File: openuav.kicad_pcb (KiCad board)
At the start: 4 copper layers, 36 x 36 mm, 68 parts, among them J1 Conn_01x01, J10 Conn_01x01, J11 Conn_01x01, J12 Conn_01x01, J13 Conn_01x01, J14 Conn_01x01, J19 Conn_01x01, J2 Conn_01x01, J20 Conn_01x01, J21 Conn_01x01, J22 Conn_01x01, J23 Conn_01x01, J24 Conn_01x01, J25 Conn_01x01, J3 Conn_01x01, J30 Conn_01x01, J31 Conn_01x01, J4 Conn_01x01, J5 Conn_01x01, J6 Conn_01x01, J7 Conn_01x01, J8 Conn_01x01, J9 Conn_01x01, J99 USB_C_Receptacle_USB2.0, SW1 SW_Push, SW2 SW_Push, U1 STM32G431CBUx, U2 LPS22HH, U3 LSM6DSR, U4 TPS54302, U6 W25N01GVZEIG, U7 TLV75733PDBV

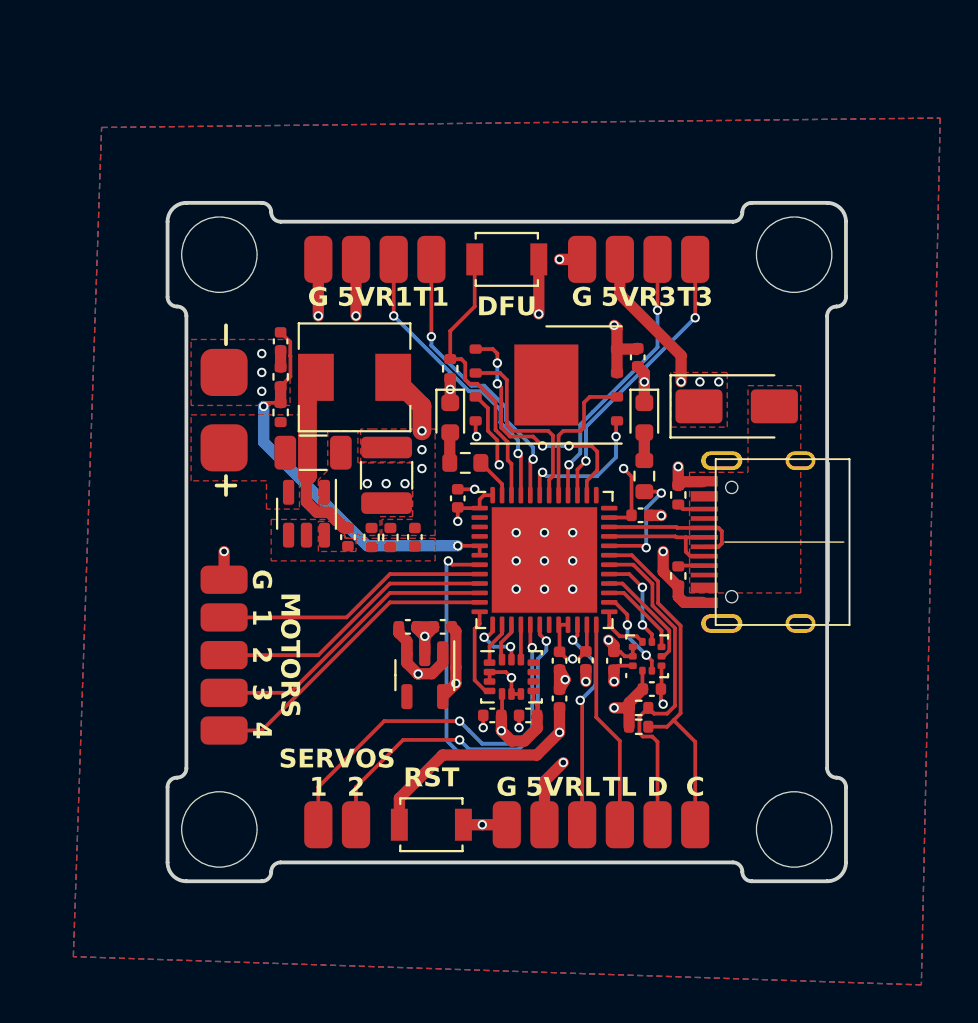
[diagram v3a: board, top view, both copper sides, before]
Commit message: Add dual 9v / 5v power supplies
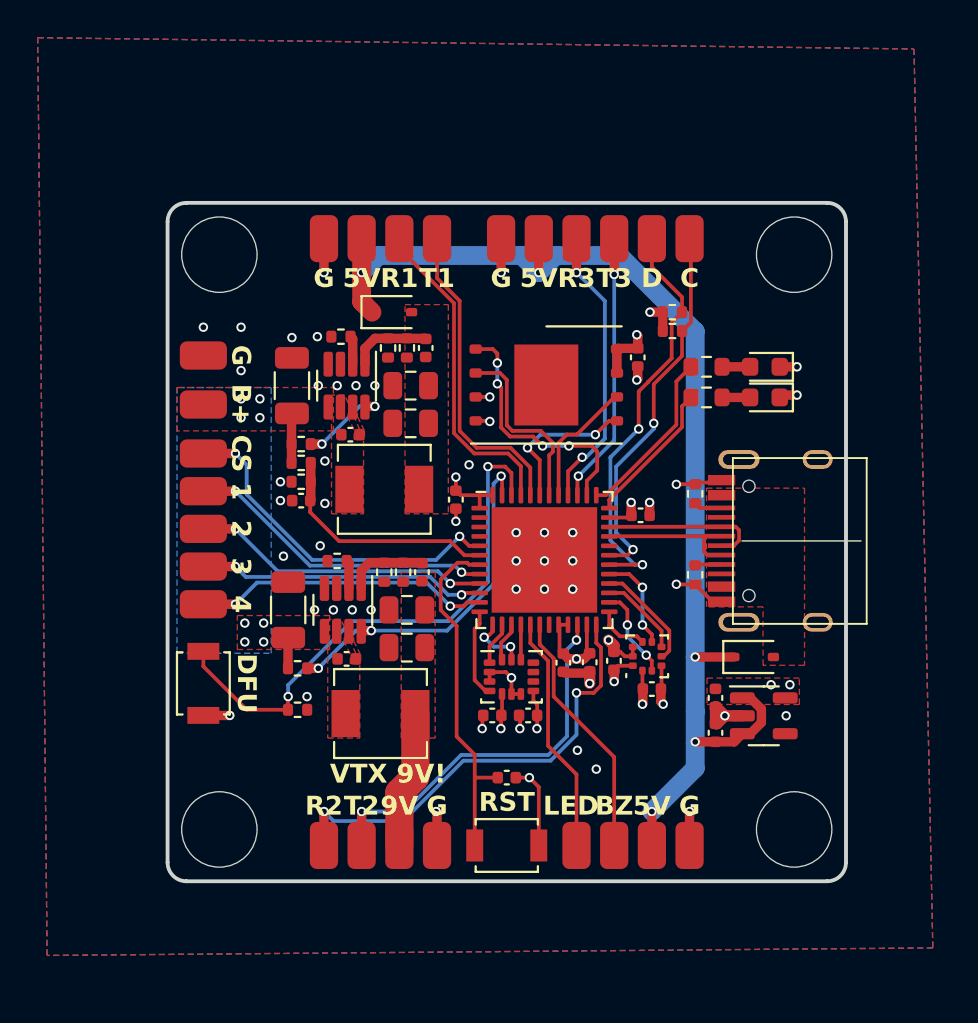
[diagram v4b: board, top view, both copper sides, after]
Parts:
- removed J30, J31: Conn_01x01, footprints:largepad
- added C17: 22u, Capacitor_SMD:C_0805_2012Metric, F.Cu at (142.7, 73.6)
- added C18: 100p, Capacitor_SMD:C_0402_1005Metric, F.Cu at (143.7, 57.7)
- added C19: 100p, Capacitor_SMD:C_0402_1005Metric, F.Cu at (143.5, 69.6)
- added C20: 22u, Capacitor_SMD:C_0805_2012Metric, F.Cu at (142.9, 61.7)
- added C21: 22u, Capacitor_SMD:C_0805_2012Metric, F.Cu at (142.7, 71.6)
- added C8: 10n, Capacitor_SMD:C_0402_1005Metric, F.Cu at (139.7, 62.3)
- added D4: PMEG2020AEA, Diode_SMD:D_SOD-323, F.Cu at (141.9, 55.8)
- added J15: Conn_01x01, footprints:smallpad, F.Cu at (131.9, 60.7)
- added J16: Conn_01x01, footprints:smallpad, F.Cu at (131.9, 58.1)
- added J17: Conn_01x01, footprints:smallpad, F.Cu at (142.3, 84.1)
- added J18: Conn_01x01, footprints:smallpad, F.Cu at (131.9, 63.3)
- added L2: 6.8u, Inductor_SMD:L_Sunlord_MWSA0402S, F.Cu at (141.3, 77.1)
- added R13: 47k, Resistor_SMD:R_0402_1005Metric, F.Cu at (139.0, 69.0)
- added R14: 100k, Resistor_SMD:R_0402_1005Metric, F.Cu at (142.5, 69.6)
- added R15: R, Resistor_SMD:R_0402_1005Metric, F.Cu at (141.5, 69.6)
- added R16: 10k, Resistor_SMD:R_0402_1005Metric, F.Cu at (137.1, 62.8)
- added R17: 10k, Resistor_SMD:R_0402_1005Metric, F.Cu at (136.9, 74.7)
- added R5: R, Resistor_SMD:R_0402_1005Metric, F.Cu at (141.7, 57.7)
- added U5: SY8303, Package_TO_SOT_SMD:TSOT-23-8, F.Cu at (139.3, 71.6)
- C10: value 68p -> 10u; footprint Capacitor_SMD:C_0402_1005Metric -> Capacitor_SMD:C_1206_3216Metric
- C15: value 47u -> 10n; footprint Capacitor_SMD:C_1210_3225Metric -> Capacitor_SMD:C_0402_1005Metric
- C9: value 100n -> 22u; footprint Capacitor_SMD:C_0402_1005Metric -> Capacitor_SMD:C_0805_2012Metric
- D1: value SS34 -> PMEG2020AEA; footprint Diode_SMD:D_SMA -> Diode_SMD:D_SOD-323
- L1: value 10u -> 6.8u; footprint Inductor_SMD:L_Sunlord_MWSA0503S -> Inductor_SMD:L_Sunlord_MWSA0402S
- R3: value 100k -> 47k
- R4: value 13.3k -> 100k
- U4: value TPS54302 -> SY8303; footprint Package_TO_SOT_SMD:SOT-23-6 -> Package_TO_SOT_SMD:TSOT-23-8
- moved J8 36.8 mm to (138.3, 84.1)
- moved J7 34.8 mm to (140.3, 84.1)
- moved J5 31.6 mm to (157.7, 84.1), turned to -90 degrees
- moved J6 31.1 mm to (155.7, 84.1), turned to -90 degrees
- moved J10 31.1 mm to (149.7, 51.9)
- moved J11 31.1 mm to (151.7, 51.9)
- moved J12 31.1 mm to (153.7, 51.9)
- moved J19 31.1 mm to (155.7, 51.9)
- moved J20 31.1 mm to (157.7, 51.9)
- moved J9 31.1 mm to (147.7, 51.9)
- moved SW1 27.7 mm to (131.9, 75.5), turned to 90 degrees
- moved R10 21.1 mm to (156.8, 56.8)
- moved R9 21.1 mm to (156.8, 55.8)
- moved R8 19.8 mm to (136.9, 76.9), turned to 0 degrees
- moved U7 18.1 mm to (161.6, 77.2), turned to 0 degrees
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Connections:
- C10 pad 1: Net-(U4-FB) -> +BATT
- C10 pad 2: +5V -> GND
- C15 pad 1: +5V -> Net-(U5-BS)
- C15 pad 2: GND -> Net-(U5-LX)
- C9 pad 1: Net-(U4-BOOT) -> Net-(D4-A)
- C9 pad 2: Net-(U4-SW) -> GND
- J11 pad 1: UART_4_RX -> UART_3_RX
- J12 pad 1: UART_4_TX -> UART_3_TX
- J7 pad 1: UART_3_RX -> UART_4_RX
- J8 pad 1: UART_3_TX -> UART_4_TX
- L1 pad 1: Net-(U4-SW) -> Net-(U4-LX)
- L1 pad 2: +5V -> Net-(D4-A)
- R3 pad 1: +5V -> Net-(U4-FS)
- R3 pad 2: Net-(U4-FB) -> GND
- R4 pad 1: Net-(U4-FB) -> Net-(D4-A)
- R4 pad 2: GND -> Net-(U4-FB)
- U1 pad 32: LED2 -> unconnected-(U1-PA10-Pad32)
- U1 pad 36: SWDIO -> LED2
- U1 pad 37: SWCLK -> LED1
- U1 pad 47: LED1 -> 9VEN
- U1 pad 5: VOLTAGE -> CURRENT
- U4 pad 1: GND -> Net-(U4-FB)
- U4 pad 2: Net-(U4-SW) -> Net-(U4-FS)
- U4 pad 3: +BATT -> GND
- U4 pad 4: Net-(U4-FB) -> GND
- U4 pad 5: unconnected-(U4-EN-Pad5) -> +BATT
- U4 pad 6: Net-(U4-BOOT) -> Net-(U4-LX)
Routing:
- net +5V: track 23.0 -> 64.4 mm, vias 9 -> 5
- net 9VEN: track 0.00 -> 19.1 mm, vias 0 -> 3
- net CURRENT: track 0.00 -> 18.7 mm, vias 0 -> 2
- net +3V3: track 39.2 -> 24.7 mm, vias 10 -> 13
- net BOOT0: track 15.0 -> 29.1 mm, vias 0 -> 2
- net UART_4_TX: track 11.1 -> 24.3 mm, vias 0 -> 2
- net NRST: track 30.8 -> 18.6 mm, vias 2 -> 0
- net UART_4_RX: track 11.6 -> 20.5 mm
- net VOLTAGE: track 21.3 -> 12.6 mm, vias 2 -> 0
- net Net-(U4-SW): track 8.70 -> 0.00 mm
- net PWM_5: track 21.2 -> 12.7 mm, vias 2 -> 0
- net +9V: track 0.00 -> 7.35 mm
- net LED1: track 2.18 -> 9.19 mm
- net PWM_6: track 19.2 -> 13.3 mm, vias 2 -> 0
- net Net-(U4-EN): track 0.00 -> 4.63 mm, vias 0 -> 2
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- added copper zone on F.Cu, net +3V3
- added copper zone on In2.Cu, net +3V3
- added copper zone on F.Cu, net +9V
- added copper zone on B.Cu, net +BATT
- added copper zone on B.Cu, net GND
- added copper zone on In1.Cu, net GND
- added copper zone on F.Cu, net Net-(D4-A)
- added copper zone on F.Cu, net Net-(U4-BS)
- added copper zone on F.Cu, net Net-(U4-LX)
- added copper zone on F.Cu, net Net-(U5-BS)
- added copper zone on F.Cu, net Net-(U5-LX)
- removed copper zone on B.Cu, net (none)
- removed copper zone on F.Cu, net (none)
- removed copper zone on In1.Cu, net +3V3
- removed copper zone on F.Cu, net +5V
- removed copper zone on In1.Cu, net +5V
- removed copper zone on In2.Cu, net GND
- removed copper zone on F.Cu, net Net-(U4-BOOT)
- removed copper zone on F.Cu, net Net-(U4-FB)
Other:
- outline, holes or cut-outs redrawn
- board text added: "9V"
- board text added: "B+"
- board text added: "BZ"
- board text added: "CS"
- board text added: "LED"
- board text added: "R2"
- board text added: "T2"
- board text added: "VTX 9V!"
- board text removed: "MOTORS"
- board text removed: "RL"
- board text removed: "SERVOS"
- board text removed: "TL"

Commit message: Add remaining part numbers, temporarily downgrade baro due to availability
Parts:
- R15: value R -> 7.15k
- R5: value R -> 13.7k
- U2: value LPS22HH -> LPS22HB
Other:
- board text added: "OPENUAV v0.3"
- board text removed: "OPENUAV v0.2"

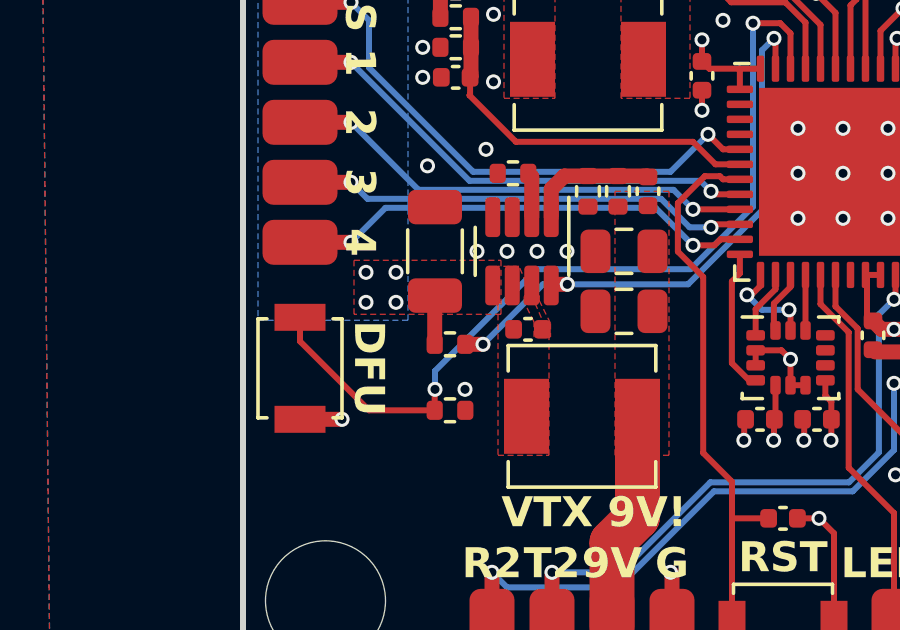
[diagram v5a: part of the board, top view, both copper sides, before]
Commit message: Change 9V enable resistor to pull-down
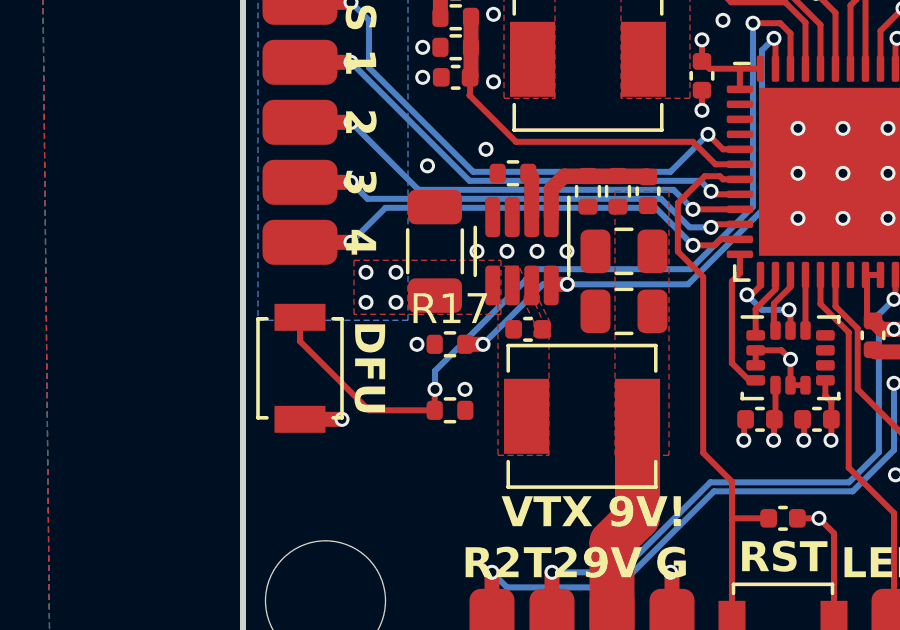
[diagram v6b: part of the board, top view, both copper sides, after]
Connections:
- R17 pad 1: +BATT -> GND
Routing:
- net +BATT: track 4.26 -> 2.63 mm
- net GND: vias 53 -> 54
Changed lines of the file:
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@@
     )
   )
+  (footprint "Resistor_SMD:R_0402_1005Metric" (layer "F.Cu")
+    (at 136.9 74.7)
+    (descr "Resistor SMD 0402 (1005 Metric), square (rectangular) end terminal, IPC_7351 nominal, (Body size source: IPC-SM-782 page 72, https://www.pcb-3d.com/wordpress/wp-content/uploads/ipc-sm-782a_amendment_1_and_2.pdf), generated with kicad-footprint-generator")
+    (tags "resistor")
+    (property "LCSC" "C25744")
+    (property "Sheetfile" "openuav.kicad_sch")
+    (property "Sheetname" "")
+    (property "ki_description" "Resistor, small symbol")
+    (property "ki_keywords" "R resistor")
+    (attr smd)
+    (fp_text reference "R17" (at 0 -1.17) (layer "F.SilkS")
+        (effects (font (size 1 1) (thickness 0.15)))
+    )
+    (fp_text value "10k" (at 0 1.17) (layer "F.Fab")
+        (effects (font (size 1 1) (thickness 0.15)))
+    )
+    (fp_text user "${REFERENCE}" (at 0 0) (layer "F.Fab")
+        (effects (font (size 0.26 0.26) (thickness 0.04)))
+    )
+    (fp_line (start -0.153641 -0.38) (end 0.153641 -0.38)
+      (stroke (width 0.12) (type solid)) (layer "F.SilkS"))
+    (fp_line (start -0.153641 0.38) (end 0.153641 0.38)
+      (stroke (width 0.12) (type solid)) (layer "F.SilkS"))
+    (fp_line (start -0.93 -0.47) (end 0.93 -0.47)
+      (stroke (width 0.05) (type solid)) (layer "F.CrtYd"))
+    (fp_line (start -0.93 0.47) (end -0.93 -0.47)
+      (stroke (width 0.05) (type solid)) (layer "F.CrtYd"))
+    (fp_line (start 0.93 -0.47) (end 0.93 0.47)
+      (stroke (width 0.05) (type solid)) (layer "F.CrtYd"))
+    (fp_line (start 0.93 0.47) (end -0.93 0.47)
+      (stroke (width 0.05) (type solid)) (layer "F.CrtYd"))
+    (fp_line (start -0.525 -0.27) (end 0.525 -0.27)
+      (stroke (width 0.1) (type solid)) (layer "F.Fab"))
+    (fp_line (start -0.525 0.27) (end -0.525 -0.27)
+      (stroke (width 0.1) (type solid)) (layer "F.Fab"))
+    (fp_line (start 0.525 -0.27) (end 0.525 0.27)
+      (stroke (width 0.1) (type solid)) (layer "F.Fab"))
+    (fp_line (start 0.525 0.27) (end -0.525 0.27)
+      (stroke (width 0.1) (type solid)) (layer "F.Fab"))
+    (pad "1" smd roundrect (at -0.51 0) (size 0.54 0.64) (layers "F.Cu" "F.Paste" "F.Mask") (roundrect_rratio 0.25)
+      (net 1 "GND") (pintype "passive"))
+    (pad "2" smd roundrect (at 0.51 0) (size 0.54 0.64) (layers "F.Cu" "F.Paste" "F.Mask") (roundrect_rratio 0.25)
+      (net 29 "9VEN") (pintype "passive"))
+    (model "${KICAD6_3DMODEL_DIR}/Resistor_SMD.3dshapes/R_0402_1005Metric.wrl"
+      (offset (xyz 0 0 0))
+      (scale (xyz 1 1 1))
+      (rotate (xyz 0 0 0))
+    )
+  )
   (footprint "footprints:smallpad" (layer "F.Cu")
     (at 144.3 84.1 90)
@@
     )
   )
-  (footprint "Resistor_SMD:R_0402_1005Metric" (layer "F.Cu")
-    (at 136.9 74.7)
-    (descr "Resistor SMD 0402 (1005 Metric), square (rectangular) end terminal, IPC_7351 nominal, (Body size source: IPC-SM-782 page 72, https://www.pcb-3d.com/wordpress/wp-content/uploads/ipc-sm-782a_amendment_1_and_2.pdf), generated with kicad-footprint-generator")
-    (tags "resistor")
-    (property "LCSC" "C25744")
-    (property "Sheetfile" "openuav.kicad_sch")
-    (property "Sheetname" "")
-    (property "ki_description" "Resistor, small symbol")
-    (property "ki_keywords" "R resistor")
-    (attr smd)
-    (fp_text reference "R17" (at 0 -1.17) (layer "F.SilkS") hide
-        (effects (font (size 1 1) (thickness 0.15)))
-    )
-    (fp_text value "10k" (at 0 1.17) (layer "F.Fab")
-        (effects (font (size 1 1) (thickness 0.15)))
-    )
-    (fp_text user "${REFERENCE}" (at 0 0) (layer "F.Fab")
-        (effects (font (size 0.26 0.26) (thickness 0.04)))
-    )
-    (fp_line (start -0.153641 -0.38) (end 0.153641 -0.38)
-      (stroke (width 0.12) (type solid)) (layer "F.SilkS"))
-    (fp_line (start -0.153641 0.38) (end 0.153641 0.38)
-      (stroke (width 0.12) (type solid)) (layer "F.SilkS"))
-    (fp_line (start -0.93 -0.47) (end 0.93 -0.47)
-      (stroke (width 0.05) (type solid)) (layer "F.CrtYd"))
-    (fp_line (start -0.93 0.47) (end -0.93 -0.47)
-      (stroke (width 0.05) (type solid)) (layer "F.CrtYd"))
-    (fp_line (start 0.93 -0.47) (end 0.93 0.47)
-      (stroke (width 0.05) (type solid)) (layer "F.CrtYd"))
-    (fp_line (start 0.93 0.47) (end -0.93 0.47)
-      (stroke (width 0.05) (type solid)) (layer "F.CrtYd"))
-    (fp_line (start -0.525 -0.27) (end 0.525 -0.27)
-      (stroke (width 0.1) (type solid)) (layer "F.Fab"))
-    (fp_line (start -0.525 0.27) (end -0.525 -0.27)
-      (stroke (width 0.1) (type solid)) (layer "F.Fab"))
-    (fp_line (start 0.525 -0.27) (end 0.525 0.27)
-      (stroke (width 0.1) (type solid)) (layer "F.Fab"))
-    (fp_line (start 0.525 0.27) (end -0.525 0.27)
-      (stroke (width 0.1) (type solid)) (layer "F.Fab"))
-    (pad "1" smd roundrect (at -0.51 0) (size 0.54 0.64) (layers "F.Cu" "F.Paste" "F.Mask") (roundrect_rratio 0.25)
-      (net 3 "+BATT") (pintype "passive"))
-    (pad "2" smd roundrect (at 0.51 0) (size 0.54 0.64) (layers "F.Cu" "F.Paste" "F.Mask") (roundrect_rratio 0.25)
-      (net 29 "9VEN") (pintype "passive"))
-    (model "${KICAD6_3DMODEL_DIR}/Resistor_SMD.3dshapes/R_0402_1005Metric.wrl"
-      (offset (xyz 0 0 0))
-      (scale (xyz 1 1 1))
-      (rotate (xyz 0 0 0))
-    )
-  )
   (footprint "MountingHole:MountingHole_4mm" locked (layer "F.Cu")
     (at 163.25 52.75)
@@
   (via (at 148.5 70.5) (size 0.5) (drill 0.3) (layers "F.Cu" "B.Cu") (net 1))
   (via (at 148.69375 77.9) (size 0.5) (drill 0.3) (layers "F.Cu" "B.Cu") (net 1))
+  (via (at 135.8 74.7) (size 0.5) (drill 0.3) (layers "F.Cu" "B.Cu") (free) (net 1))
   (via (at 138.35 63.7) (size 0.5) (drill 0.3) (layers "F.Cu" "B.Cu") (free) (net 1))
   (via (at 133.9 56.6) (size 0.5) (drill 0.3) (layers "F.Cu" "B.Cu") (free) (net 1))
@@
   (segment (start 136.58 62.8) (end 136.58 61.195) (width 0.5) (layer "F.Cu") (net 3))
   (segment (start 136.58 61.195) (end 136.6 61.175) (width 0.5) (layer "F.Cu") (net 3))
-  (segment (start 136.39 74.7) (end 136.39 73.085) (width 0.5) (layer "F.Cu") (net 3))
-  (segment (start 136.39 73.085) (end 136.4 73.075) (width 0.5) (layer "F.Cu") (net 3))
   (segment (start 136.58 63.8) (end 136.58 62.8) (width 0.5) (layer "F.Cu") (net 3))
   (via (at 134.1 73.3) (size 0.5) (drill 0.3) (layers "F.Cu" "B.Cu") (net 3))
@@
   (segment (start 153.7 84.1) (end 153.7 79.41) (width 0.2) (layer "F.Cu") (net 28))
   (segment (start 153.7 79.41) (end 150.49 76.2) (width 0.2) (layer "F.Cu") (net 28))
-  (segment (start 137.41 74.7) (end 138 74.7) (width 0.5) (layer "F.Cu") (net 29))
   (segment (start 147.75 65.5125) (end 147.75 64.55) (width 0.2) (layer "F.Cu") (net 29))
   (segment (start 140.81 72.7) (end 140.41 72.7) (width 0.5) (layer "F.Cu") (net 29))
   (segment (start 147.75 64.55) (end 147.7 64.5) (width 0.2) (layer "F.Cu") (net 29))
+  (segment (start 138 74.7) (end 137.41 74.7) (width 0.5) (layer "F.Cu") (net 29))
   (via (at 147.7 64.5) (size 0.5) (drill 0.3) (layers "F.Cu" "B.Cu") (net 29))
   (via (at 140.81 72.7) (size 0.5) (drill 0.3) (layers "F.Cu" "B.Cu") (net 29))
